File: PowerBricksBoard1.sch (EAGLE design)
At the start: 11 parts

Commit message: Board with draft routing
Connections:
- net 12V renamed G
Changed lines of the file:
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@@
 <?xml version="1.0" encoding="utf-8"?>
 <!DOCTYPE eagle SYSTEM "eagle.dtd">
-<eagle version="9.5.0">
+<eagle version="9.3.0">
 <drawing>
 <settings>
@@
 </segment>
 </net>
-<net name="12V" class="0">
+<net name="G" class="0">
 <segment>
 <wire x1="17.78" y1="20.32" x2="33.02" y2="20.32" width="0.1524" layer="91"/>

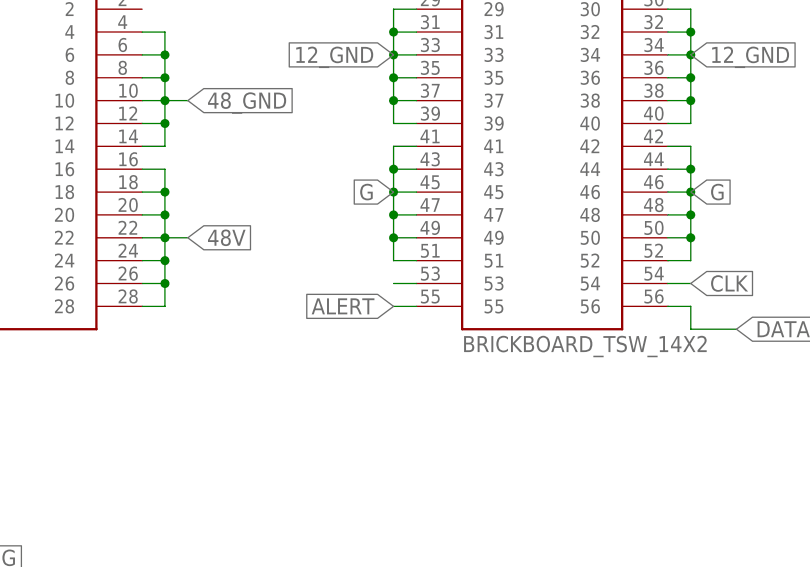
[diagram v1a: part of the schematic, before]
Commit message: Fixed DRC error
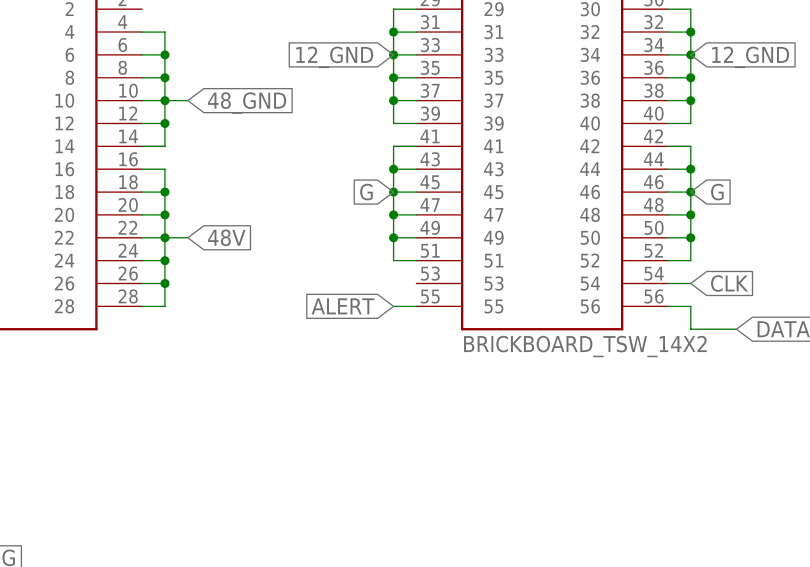
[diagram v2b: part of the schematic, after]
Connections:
- removed net N$14: U$5.53
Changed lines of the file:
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@@
-</segment>
-</net>
-<net name="N$14" class="0">
-<segment>
-<pinref part="U$5" gate="G$1" pin="53"/>
-<wire x1="81.28" y1="50.8" x2="78.74" y2="50.8" width="0.1524" layer="91"/>
 </segment>
 </net>
@@
 </sheet>
 </sheets>
+<errors>
+</errors>
 </schematic>
 </drawing>
